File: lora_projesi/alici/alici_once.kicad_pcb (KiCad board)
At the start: 4 copper layers, 84 x 98 mm, 127 parts, among them J1 USB-C, J2 SMA, J3 RJ45, J4 u.FL (ANA ANTEN), J5 12 V GIRIS, J6 LAMBA, J7 MICRO-SIM, J8 u.FL (YARDIMCI ANTEN, ISTEGE 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, K1 SRD-12VDC-SL-A, Q1 AO3401A, Q2 MMBT2222A, Q3 MMBT2222A, Q4 MMBT2222A, SW1 DUGME, U1 ESP32-S3-WROOM-1-N4, U10 SIM7600SA, U11 AP2112K-3.3, U12 ESDA6V1-5SC6, U4 RFM95W-915S2, U5 TPS62933DRLR, U6 TPS62933DRLR, U7 USBLC6-2SC6, U8 TXB0104PW, U9 W5500, Y1 25 MHz

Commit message: Alici: yerlesim duzeltmesi (calisma durumu)
Co-Authored-By: Claude Sonnet 5.5 <noreply@anthropic.com>
Claude-Session: https://claude.ai/code/session_01Q71gHQtKJ86ZE2CtYTYSwP
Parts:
- moved C37 25.3 mm to (52.7, 75.7)
- moved C38 25.2 mm to (53.4, 78.3), turned to 90 degrees
- moved C33 23.2 mm to (55.4, 76.2)
- moved C32 20.4 mm to (51.7, 73.8), turned to 0 degrees
- moved C31 17.2 mm to (55.0, 72.7), turned to 90 degrees
- moved C29 15.2 mm to (55.4, 55.1), turned to 90 degrees
- moved D3 11.3 mm to (43.0, 81.9), turned to 0 degrees
- moved C16 10.6 mm to (44.4, 70.8)
- moved R26 10.5 mm to (49.0, 72.9), turned to 90 degrees
- moved C30 9.57 mm to (52.4, 72.0)
- moved R11 6.32 mm to (30.7, 85.1)
- moved SW1 6.32 mm to (36.0, 86.0)
- moved R7 6.08 mm to (28.9, 74.8)
- moved C11 6.08 mm to (36.3, 73.2)
- moved C12 6.08 mm to (33.2, 70.7)
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
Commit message: Alıcı kartı: yol çizimi iyileştirmesi, U9 toprak ayakları ön yerleşim, düzeltme betiği
Co-Authored-By: Claude Sonnet 5.5 <noreply@anthropic.com>
Claude-Session: https://claude.ai/code/session_01Q71gHQtKJ86ZE2CtYTYSwP
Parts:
- moved C27 19.5 mm to (47.5, 50.8), turned to 90 degrees
- moved C51 18.5 mm to (39.9, 68.2), turned to 90 degrees
- moved C50 15.5 mm to (40.7, 64.7)
- moved R21 13.6 mm to (46.4, 56.3), turned to 90 degrees
- moved C29 13.0 mm to (55.6, 68.2), turned to 0 degrees
- moved C25 12.4 mm to (45.6, 52.7), turned to 90 degrees
- moved R35 11.9 mm to (43.9, 64.7), turned to 0 degrees
- moved R29 10.9 mm to (53.6, 51.4), turned to 0 degrees
- moved R19 6.94 mm to (46.4, 63.5)
- moved R27 5.51 mm to (60.3, 52.4), turned to 0 degrees
- moved R16 4.94 mm to (47.9, 59.7), turned to 90 degrees
- moved C34 4.74 mm to (57.1, 55.8)
- moved R18 4.09 mm to (46.1, 60.0)
- moved R15 3.87 mm to (49.2, 63.0), turned to 0 degrees
- moved C28 3.18 mm to (53.7, 53.8)
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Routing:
- net GND: track 0.00 -> 93.7 mm, vias 0 -> 9
- net +3V3: track 0.00 -> 1.10 mm, vias 0 -> 1

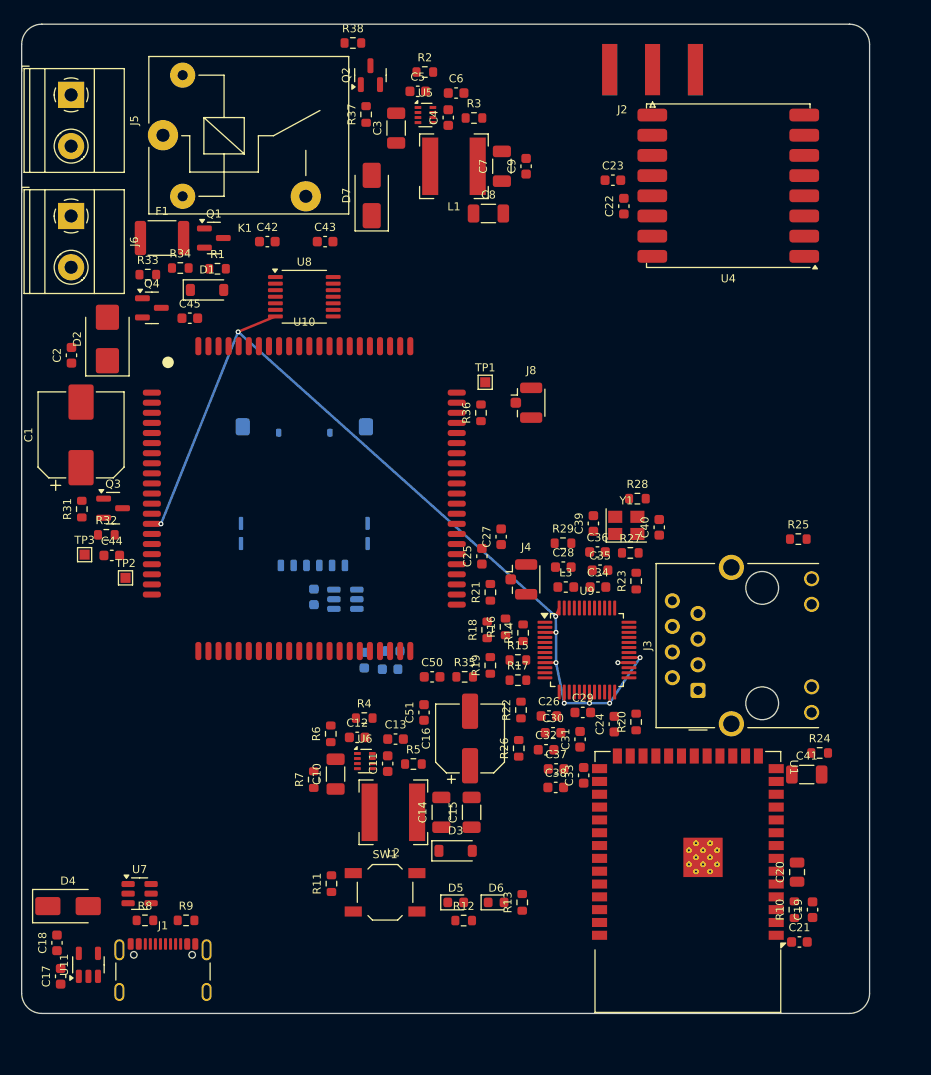
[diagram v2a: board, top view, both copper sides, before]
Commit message: Ders sitesi: şema çizici (bağlantı listesiyle denetimli), kart görüntüleyici, hesap makineleri, verici besleme bölümü, otomatik yayın
Co-Authored-By: Claude Sonnet 5.5 <noreply@anthropic.com>
Claude-Session: https://claude.ai/code/session_01Q71gHQtKJ86ZE2CtYTYSwP
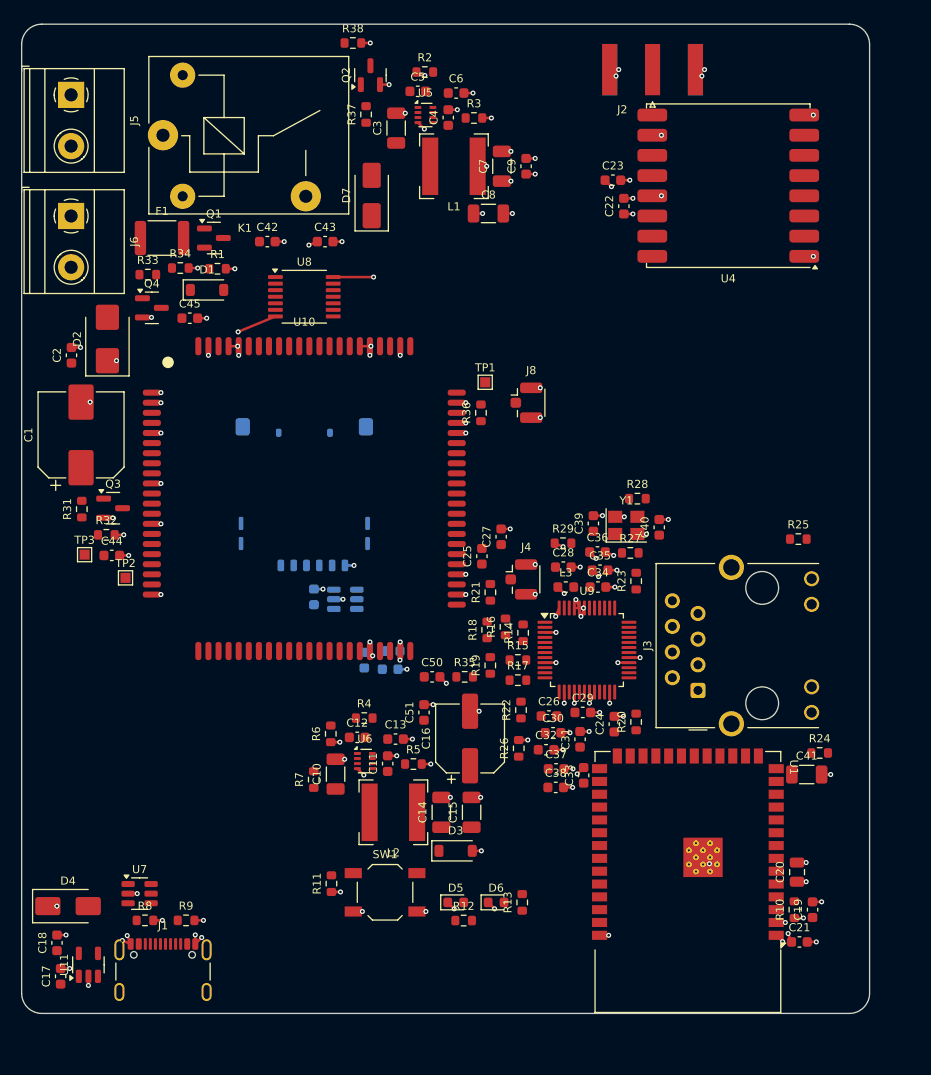
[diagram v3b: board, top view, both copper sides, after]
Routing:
- net +3V3: track 1.10 -> 25.8 mm, vias 1 -> 25
- net GND: track 93.7 -> 111.8 mm, vias 9 -> 119

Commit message: Alici: yerlesim boslugu artirildi, kart 88x102 (yol cizimi suruyor)
Co-Authored-By: Claude Sonnet 5.5 <noreply@anthropic.com>
Claude-Session: https://claude.ai/code/session_01Q71gHQtKJ86ZE2CtYTYSwP
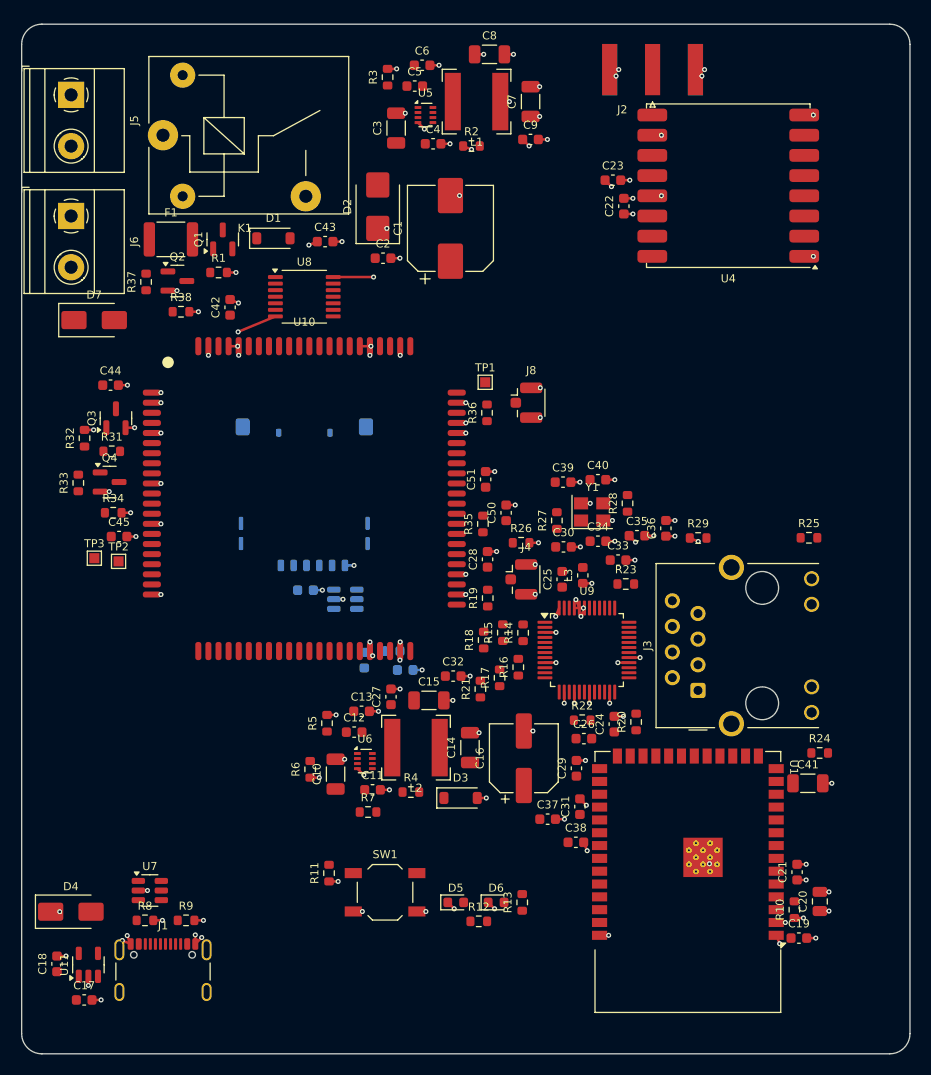
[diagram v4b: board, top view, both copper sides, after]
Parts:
- moved C1 41.9 mm to (42.5, 20.2)
- moved C2 32.3 mm to (35.8, 23.2), turned to 0 degrees
- moved R38 31.6 mm to (15.8, 28.5)
- moved D7 30.1 mm to (7.18, 29.3), turned to 0 degrees
- moved D2 29.8 mm to (35.3, 18.1)
- moved Q2 28.0 mm to (15.4, 25.4), turned to 0 degrees
- moved R37 27.4 mm to (12.3, 25.5)
- moved R34 25.1 mm to (9.07, 48.4)
- moved C51 23.9 mm to (46.0, 45.1)
- moved C45 22.7 mm to (9.65, 50.8)
- moved R33 21.8 mm to (5.61, 45.4), turned to 90 degrees
- moved C33 21.6 mm to (59.1, 53.1), turned to 0 degrees
- moved R26 20.4 mm to (49.5, 51.4), turned to 0 degrees
- moved C27 19.2 mm to (36.6, 66.6)
- moved C30 18.4 mm to (53.7, 51.8)
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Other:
- board size 84 x 98 mm -> 88 x 102 mm

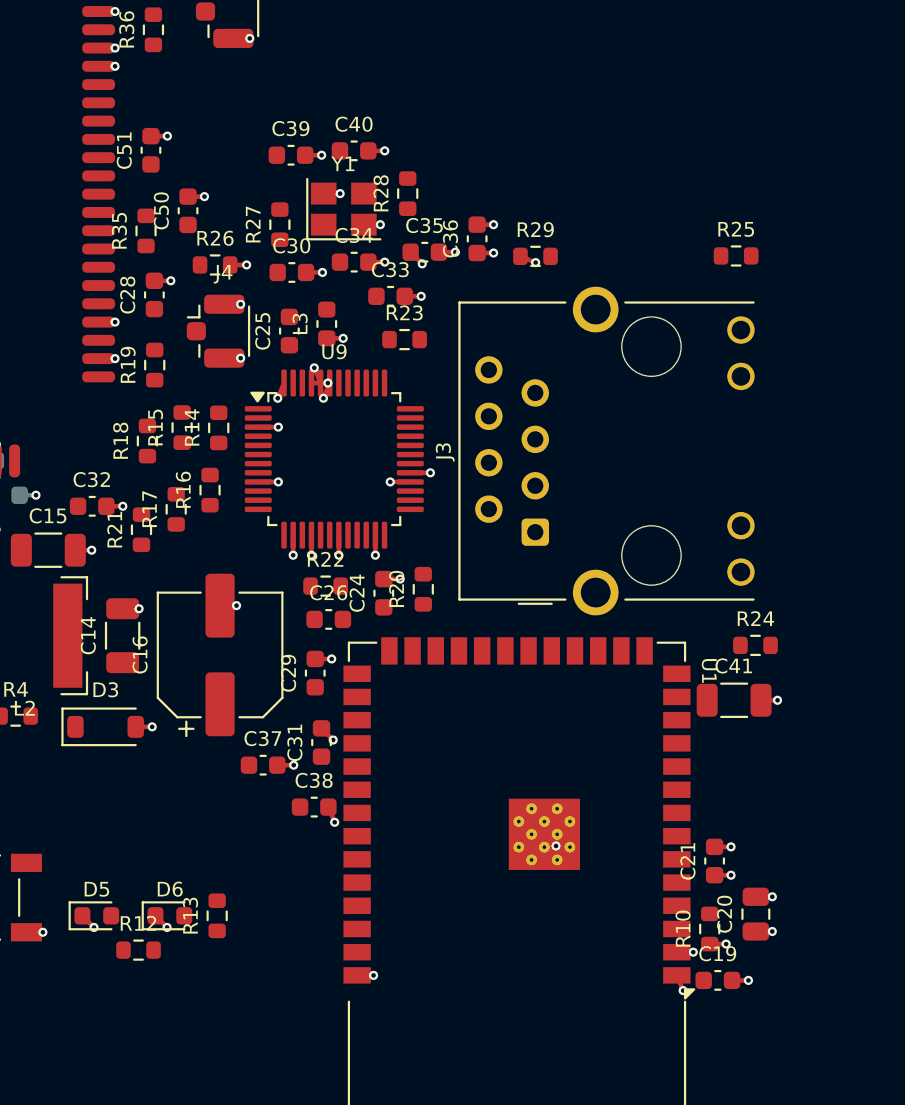
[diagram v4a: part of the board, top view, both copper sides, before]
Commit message: Alici: kupe poligonu ile yerlesim, izgara yonlendirici (izgara.py)
Co-Authored-By: Claude Sonnet 5.5 <noreply@anthropic.com>
Claude-Session: https://claude.ai/code/session_01Q71gHQtKJ86ZE2CtYTYSwP
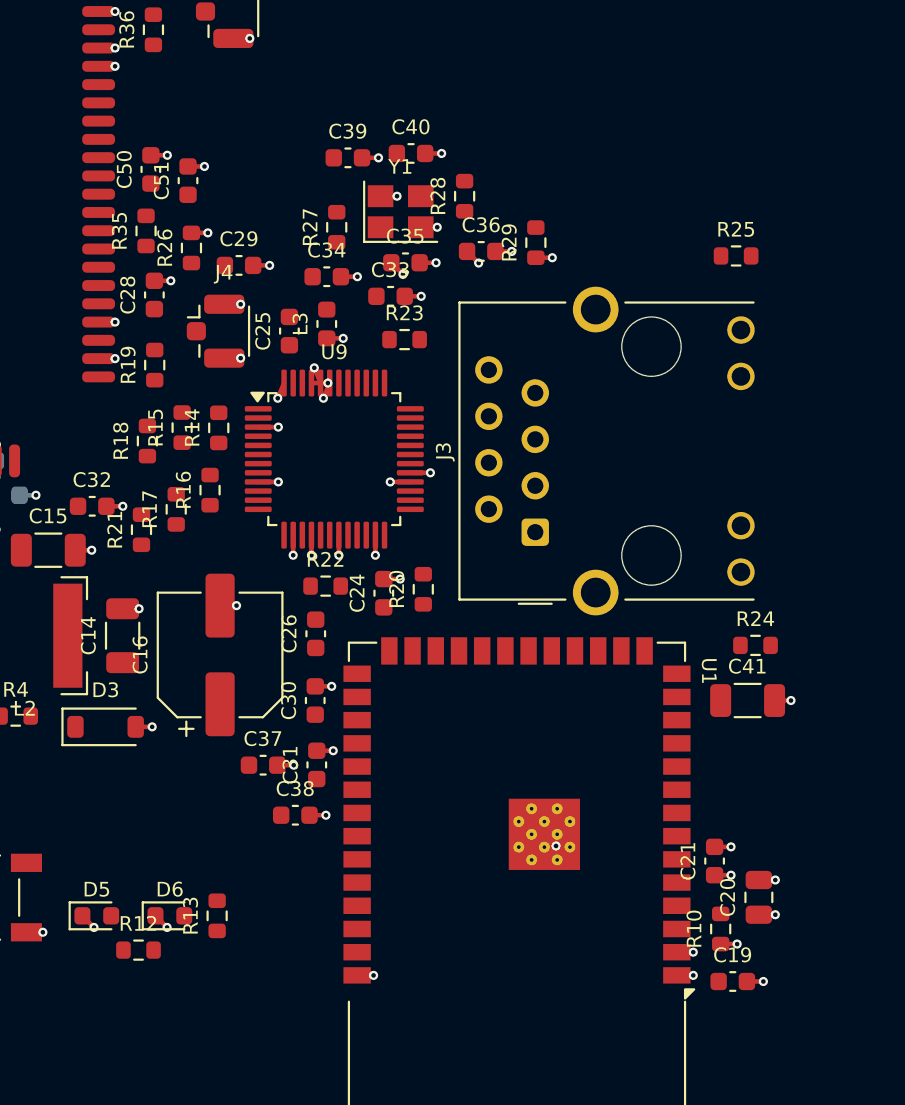
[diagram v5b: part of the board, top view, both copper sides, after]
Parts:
- moved C30 23.5 mm to (55.0, 75.2), turned to 90 degrees
- moved C29 22.7 mm to (50.8, 51.4), turned to 0 degrees
- moved R28 3.12 mm to (63.1, 47.6)
- moved C39 3.12 mm to (56.7, 45.5)
- moved C40 3.12 mm to (60.2, 45.3)
- moved R27 3.12 mm to (56.1, 49.3)
- moved Y1 3.12 mm to (59.6, 48.5)
- moved C50 3.04 mm to (46.0, 46.1)
- moved C51 2.62 mm to (48.0, 46.8)
- moved C34 1.70 mm to (55.6, 52.0)
- moved R26 1.59 mm to (48.2, 50.4), turned to 90 degrees
- moved C31 1.25 mm to (55.0, 78.7)
- moved C35 1.20 mm to (59.9, 51.3)
- moved C38 1.13 mm to (53.9, 81.5)
- moved C26 1.06 mm to (55.0, 71.6), turned to 90 degrees
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
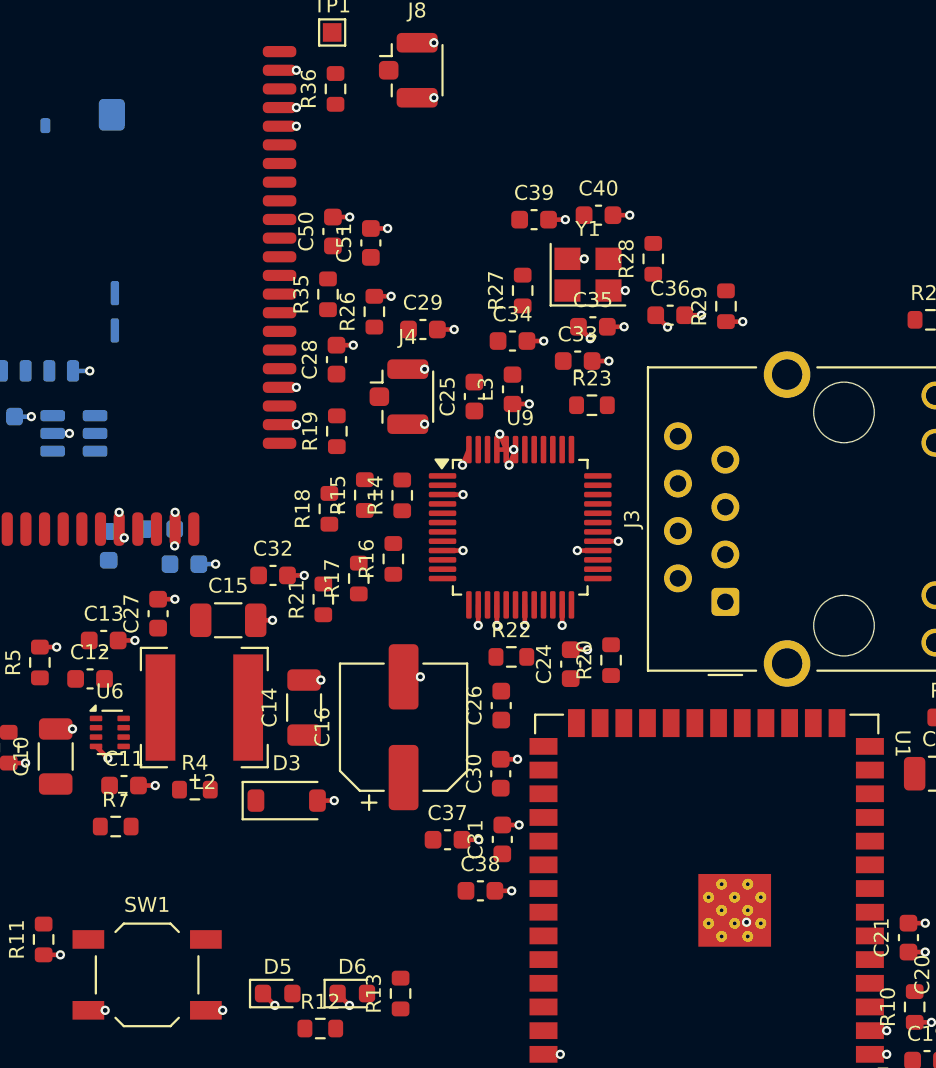
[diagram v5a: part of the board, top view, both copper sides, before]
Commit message: Alici: ETH cevresi icin genis yerlesim aralagi (yonlendirme suruyor)
Co-Authored-By: Claude Sonnet 5.5 <noreply@anthropic.com>
Claude-Session: https://claude.ai/code/session_01Q71gHQtKJ86ZE2CtYTYSwP
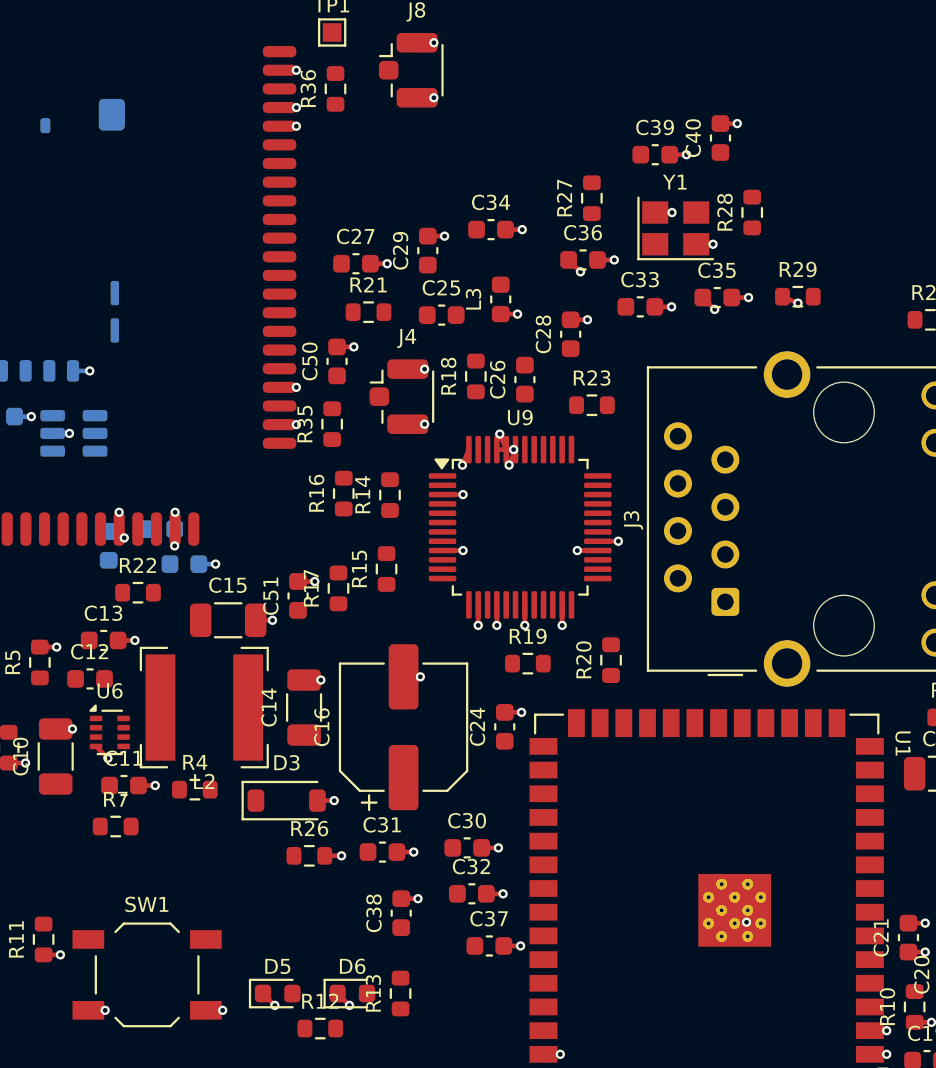
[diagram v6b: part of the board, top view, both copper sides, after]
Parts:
- moved R26 29.4 mm to (44.7, 79.6), turned to 0 degrees
- moved C27 21.6 mm to (47.2, 47.9), turned to 0 degrees
- moved R22 20.3 mm to (35.5, 65.5)
- moved C32 20.1 mm to (53.4, 81.7)
- moved C51 19.3 mm to (44.1, 65.7)
- moved C26 17.5 mm to (56.3, 54.1)
- moved R19 16.1 mm to (56.4, 69.3), turned to 0 degrees
- moved R21 15.6 mm to (47.9, 50.5), turned to 0 degrees
- moved C28 12.6 mm to (58.7, 51.7)
- moved R18 10.6 mm to (53.6, 53.9)
- moved C40 7.74 mm to (66.7, 41.1), turned to 90 degrees
- moved C39 7.37 mm to (63.2, 42.0)
- moved R35 6.97 mm to (45.9, 56.5)
- moved C50 6.97 mm to (46.2, 53.1)
- moved C35 6.85 mm to (66.6, 49.7)
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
